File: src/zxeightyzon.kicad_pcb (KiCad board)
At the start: 2 copper layers, 77.6 x 75.9 mm, 0 parts

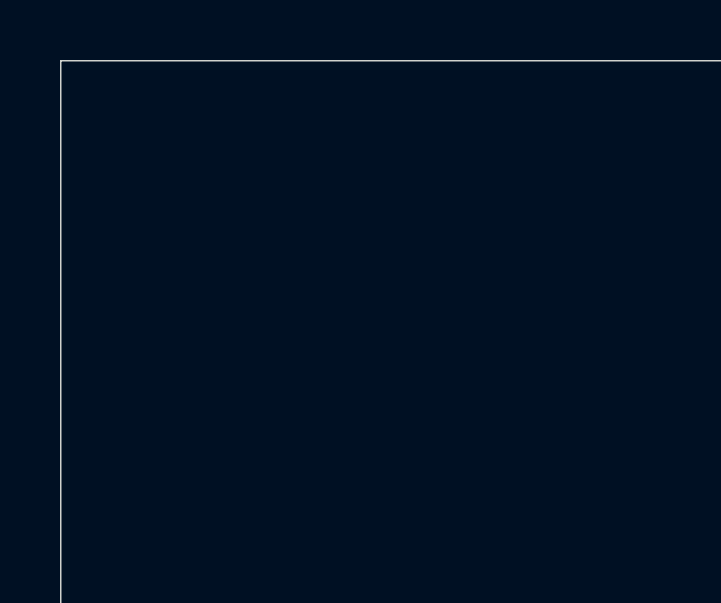
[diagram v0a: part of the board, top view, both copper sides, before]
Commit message: added logo footprint
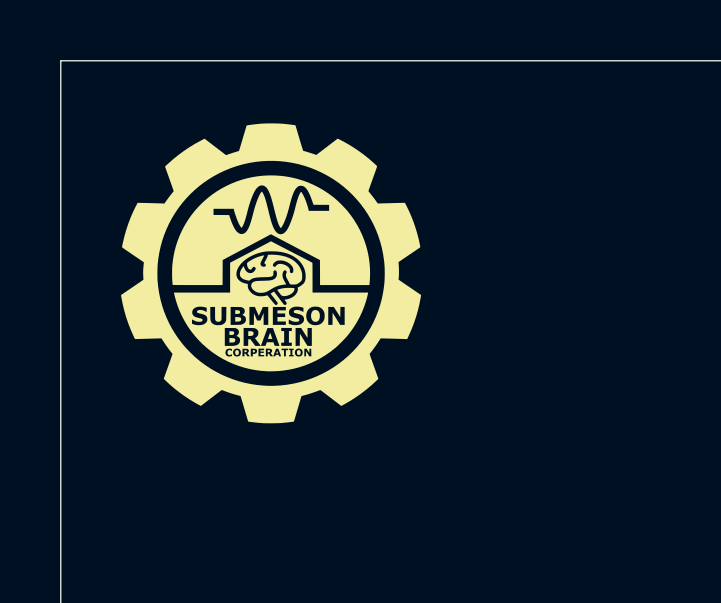
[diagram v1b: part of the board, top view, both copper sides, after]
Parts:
- added G***: LOGO, SBCLogo:SBCLogo, F.Cu at (57.7, 32.8)

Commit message: started PCB layout
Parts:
- added C1: 10uf, Capacitor_THT:CP_Radial_D5.0mm_P2.00mm, B.Cu at (218.8, 64.1)
- added C2: 10uf, Capacitor_THT:CP_Radial_D5.0mm_P2.00mm, B.Cu at (218.6, 54.0)
- added C3: 100nf, Capacitor_THT:C_Disc_D3.0mm_W1.6mm_P2.50mm, B.Cu at (238.3, 64.1)
- added C4: 100nf, Capacitor_THT:C_Disc_D3.0mm_W1.6mm_P2.50mm, B.Cu at (238.3, 54.0)
- added C5: 100nf, Capacitor_THT:C_Disc_D3.0mm_W1.6mm_P2.50mm, B.Cu at (199.9, 92.9)
- added C6: 100nf, Capacitor_THT:C_Disc_D3.0mm_W1.6mm_P2.50mm, B.Cu at (180.0, 108.3)
- added CO1: Connector ZX81, ZX81_Expansion_Connector:ZX81_EdgeConnector, F.Cu at (222.9, 104.3)
- added CO2: LINEOUT, audio_jack:CONN5_SPC21348_MTC, B.Cu at (244.3, 54.0)
- added FB1: FB, Resistor_THT:R_Axial_DIN0207_L6.3mm_D2.5mm_P7.62mm_Horizontal, B.Cu at (197.7, 77.7)
- added J1: 01x10, Connector_PinHeader_2.54mm:PinHeader_1x10_P2.54mm_Vertical, B.Cu at (250.8, 71.9)
- added J2: 01x10, Connector_PinHeader_2.54mm:PinHeader_1x10_P2.54mm_Vertical, B.Cu at (224.4, 71.9)
- added J3: 01x10, Connector_PinHeader_2.54mm:PinHeader_1x10_P2.54mm_Vertical, B.Cu at (198.0, 71.9)
- added J4: Conn_02x02_Top_Bottom, Connector_PinHeader_2.54mm:PinHeader_2x02_P2.54mm_Vertical, B.Cu at (197.1, 56.7)
- added JP1: YM 1/2 CLK, Connector_PinHeader_2.54mm:PinHeader_1x02_P2.54mm_Vertical, B.Cu at (194.2, 90.4)
- added JP2: CLK Select, Connector_PinHeader_2.54mm:PinHeader_1x03_P2.54mm_Vertical, B.Cu at (190.5, 90.4)
- added R2: 390R, Resistor_THT:R_Axial_DIN0207_L6.3mm_D2.5mm_P7.62mm_Horizontal, B.Cu at (205.3, 64.1)
- added R3: 390R, Resistor_THT:R_Axial_DIN0207_L6.3mm_D2.5mm_P7.62mm_Horizontal, B.Cu at (205.3, 54.0)
- added R4: 820R, Resistor_THT:R_Axial_DIN0207_L6.3mm_D2.5mm_P7.62mm_Horizontal, B.Cu at (212.9, 61.1)
- added R5: 820R, Resistor_THT:R_Axial_DIN0207_L6.3mm_D2.5mm_P7.62mm_Horizontal, B.Cu at (212.9, 57.0)
- added R6: 390R, Resistor_THT:R_Axial_DIN0207_L6.3mm_D2.5mm_P7.62mm_Horizontal, B.Cu at (226.7, 60.9)
- added R7: 390R, Resistor_THT:R_Axial_DIN0207_L6.3mm_D2.5mm_P7.62mm_Horizontal, B.Cu at (226.7, 57.0)
- added R8: 100R, Resistor_THT:R_Axial_DIN0207_L6.3mm_D2.5mm_P7.62mm_Horizontal, B.Cu at (226.7, 64.1)
- added R9: 100R, Resistor_THT:R_Axial_DIN0207_L6.3mm_D2.5mm_P7.62mm_Horizontal, B.Cu at (226.7, 54.0)
- added U1: YM2149, Package_DIP:DIP-40_W15.24mm_LongPads, B.Cu at (202.6, 77.7)
- added U2: GAL22V10, Package_DIP:DIP-24_W7.62mm_LongPads, B.Cu at (182.5, 77.7)
- G***: moved to B.Cu
- moved G*** 128.6 mm to (183.5, 59.4), turned to 180 degrees
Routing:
- net VCC: track 0.00 -> 181.2 mm
- net GND: track 0.00 -> 177.0 mm
- net /BDIR: track 0.00 -> 86.9 mm, vias 0 -> 1
- net /A7: track 0.00 -> 84.0 mm, vias 0 -> 2
- net GND_AUDIO: track 0.00 -> 83.6 mm, vias 0 -> 1
- net /A4: track 0.00 -> 82.5 mm, vias 0 -> 1
- net /A6: track 0.00 -> 79.9 mm, vias 0 -> 1
- net /A5: track 0.00 -> 76.6 mm, vias 0 -> 2
- net Net-(JP2-C): track 0.00 -> 62.4 mm
- net /~{RD}: track 0.00 -> 61.7 mm
- net /BC1: track 0.00 -> 59.7 mm
- net /A0: track 0.00 -> 57.0 mm, vias 0 -> 2
- net /CLK: track 0.00 -> 56.2 mm, vias 0 -> 1
- net /~{WR}: track 0.00 -> 54.8 mm
- net /A2: track 0.00 -> 54.6 mm, vias 0 -> 1
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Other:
- board size 77.6 x 75.9 mm -> 82.2 x 62 mm

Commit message: fab files
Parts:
- moved C2 134.5 mm to (84.9, 39.5)
- moved C6 134.5 mm to (46.2, 93.8)
- moved R6 134.5 mm to (93.0, 46.4)
- moved R7 134.5 mm to (93.0, 42.5)
- moved R8 134.5 mm to (93.0, 49.6)
- moved R9 134.5 mm to (93.0, 39.5)
- moved C3 134.5 mm to (104.5, 49.6)
- moved C4 134.5 mm to (104.5, 39.5)
- moved C5 134.5 mm to (66.2, 78.5)
- moved CO1 134.5 mm to (89.1, 89.8)
- moved FB1 134.5 mm to (64.0, 63.2)
- moved J2 134.5 mm to (90.7, 57.4)
- moved J3 134.5 mm to (64.3, 57.4)
- moved J4 134.5 mm to (63.4, 42.3)
- moved JP1 134.5 mm to (60.4, 75.9)
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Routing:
- net /A7: track 84.0 -> 63.9 mm, vias 2 -> 0
- net /BDIR: track 86.9 -> 68.2 mm
- net VCC: track 181.2 -> 194.2 mm
- net /D5: track 26.1 -> 17.8 mm
- net /A5: track 76.6 -> 69.9 mm, vias 2 -> 0
- net /D3: track 9.82 -> 16.3 mm
- net /IOA0: track 23.1 -> 29.0 mm
- net /A6: track 79.9 -> 85.7 mm
- net Net-(J4-Pin_2): track 6.75 -> 11.6 mm
- net /A0: track 57.0 -> 52.2 mm, vias 2 -> 1
- net /IOA4: track 12.7 -> 7.95 mm
- net /IOA2: track 12.7 -> 7.95 mm
- net /IOA7: track 8.38 -> 12.7 mm
- net /A2: track 54.6 -> 50.6 mm
- net /IOA5: track 11.4 -> 7.95 mm
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
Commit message: Added silkscreen overlays
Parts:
- J1 I/O-A: renamed from J1
- J2 I/O-B: renamed from J2
- J3 GAL: renamed from J3
- moved G*** 5.03 mm to (45.2, 42.8)
- renumbered J4 to ABC↓, JP2 to CLK, JP1 to SEL
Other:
- board text added: "ACB→"
- board text added: "CLK/2"
- board text added: "ZXEightyZON rev 1.0 Designed by Bambleweeny57 for Submeson Brain Corporation"
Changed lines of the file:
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@@
 		(descr "Through hole straight pin header, 2x02, 2.54mm pitch, double rows")
 		(tags "Through hole pin header THT 2x02 2.54mm double row")
-		(property "Reference" "J4"
-			(at 1.397 2.413 0)
+		(property "Reference" "ABC↓"
+			(at 1.1094 2.4914 0)
 			(layer "B.SilkS")
 			(effects
@@
 		(descr "Through hole straight pin header, 1x02, 2.54mm pitch, single row")
 		(tags "Through hole pin header THT 1x02 2.54mm single row")
-		(property "Reference" "JP1"
+		(property "Reference" "SEL"
 			(at 0 2.54 0)
 			(layer "B.SilkS")
@@
 		(descr "Through hole straight pin header, 1x10, 2.54mm pitch, single row")
 		(tags "Through hole pin header THT 1x10 2.54mm single row")
-		(property "Reference" "J2"
-			(at 2.413 0 0)
+		(property "Reference" "J2 I/O-B"
+			(at 2.3932 -2.4202 0)
 			(layer "B.SilkS")
 			(effects
@@
 		(descr "Through hole straight pin header, 1x10, 2.54mm pitch, single row")
 		(tags "Through hole pin header THT 1x10 2.54mm single row")
-		(property "Reference" "J1"
-			(at 2.413 0 0)
+		(property "Reference" "J1 I/O-A"
+			(at 2.3932 -2.3362 0)
 			(layer "B.SilkS")
 			(effects
@@
 		(descr "Through hole straight pin header, 1x10, 2.54mm pitch, single row")
 		(tags "Through hole pin header THT 1x10 2.54mm single row")
-		(property "Reference" "J3"
-			(at 2.413 0 0)
+		(property "Reference" "J3 GAL"
+			(at 2.3932 -1.2542 0)
 			(layer "B.SilkS")
 			(effects
@@
 	(footprint "SBCLogo:SBCLogo"
 		(layer "B.Cu")
-		(at 49.7762 44.9472 180)
+		(at 45.25 42.75 180)
 		(property "Reference" "G***"
 			(at 0 0 0)
@@
 		(descr "Through hole straight pin header, 1x03, 2.54mm pitch, single row")
 		(tags "Through hole pin header THT 1x03 2.54mm single row")
-		(property "Reference" "JP2"
+		(property "Reference" "CLK"
 			(at 0 2.54 0)
 			(layer "B.SilkS")
@@
 		(layer "Edge.Cuts")
 	)
+	(gr_text "ACB→"
+		(at 66.25 37.75 0)
+		(layer "B.SilkS")
+		(effects
+			(font
+				(size 1 1)
+				(thickness 0.15)
+			)
+			(justify left bottom mirror)
+		)
+	)
+	(gr_text "CLK/2"
+		(at 58.25 84 0)
+		(layer "B.SilkS")
+		(effects
+			(font
+				(size 1 1)
+				(thickness 0.15)
+			)
+			(justify left bottom mirror)
+		)
+	)
+	(gr_text "ZXEightyZON rev 1.0\nDesigned by Bambleweeny57\nfor Submeson Brain Corporation"
+		(at 67 52 0)
+		(layer "B.SilkS")
+		(effects
+			(font
+				(size 1 1)
+				(thickness 0.1)
+			)
+			(justify left bottom mirror)
+		)
+	)
 	(segment

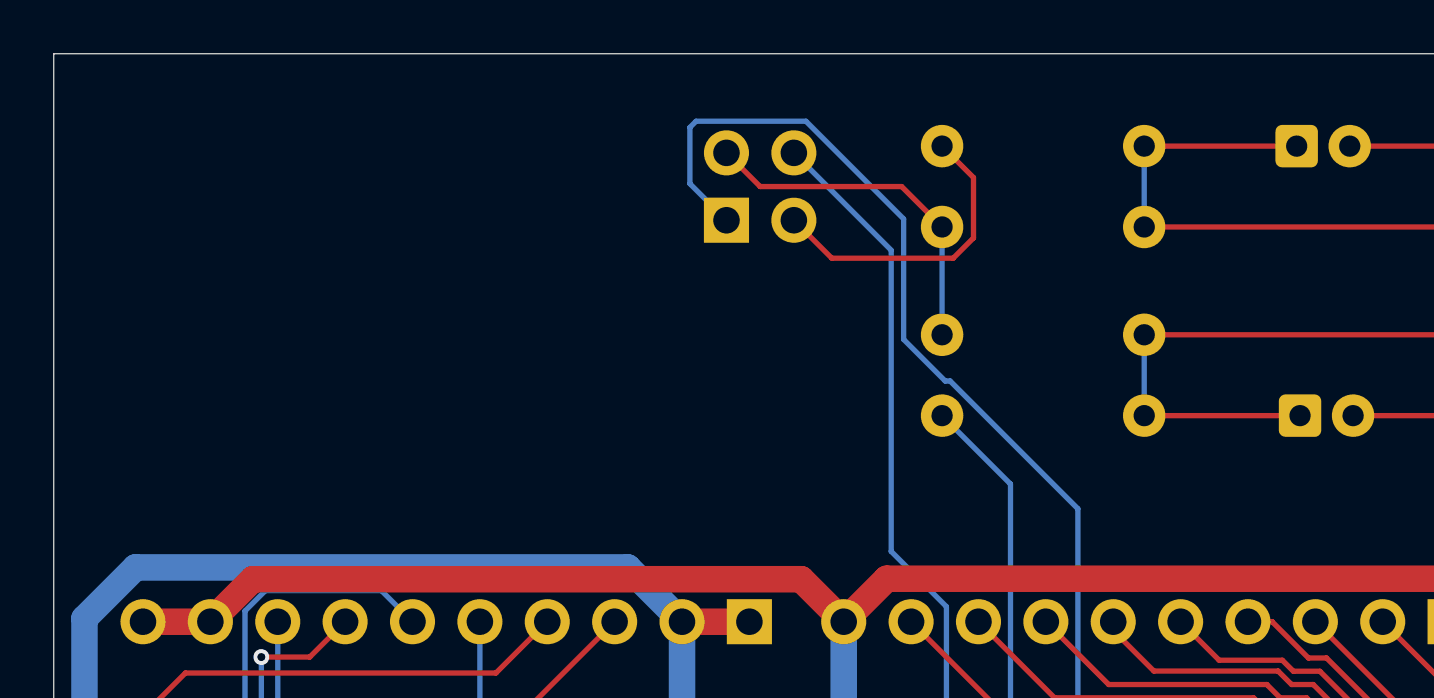
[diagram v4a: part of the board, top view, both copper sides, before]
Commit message: Added Open Hardware Silk Screen
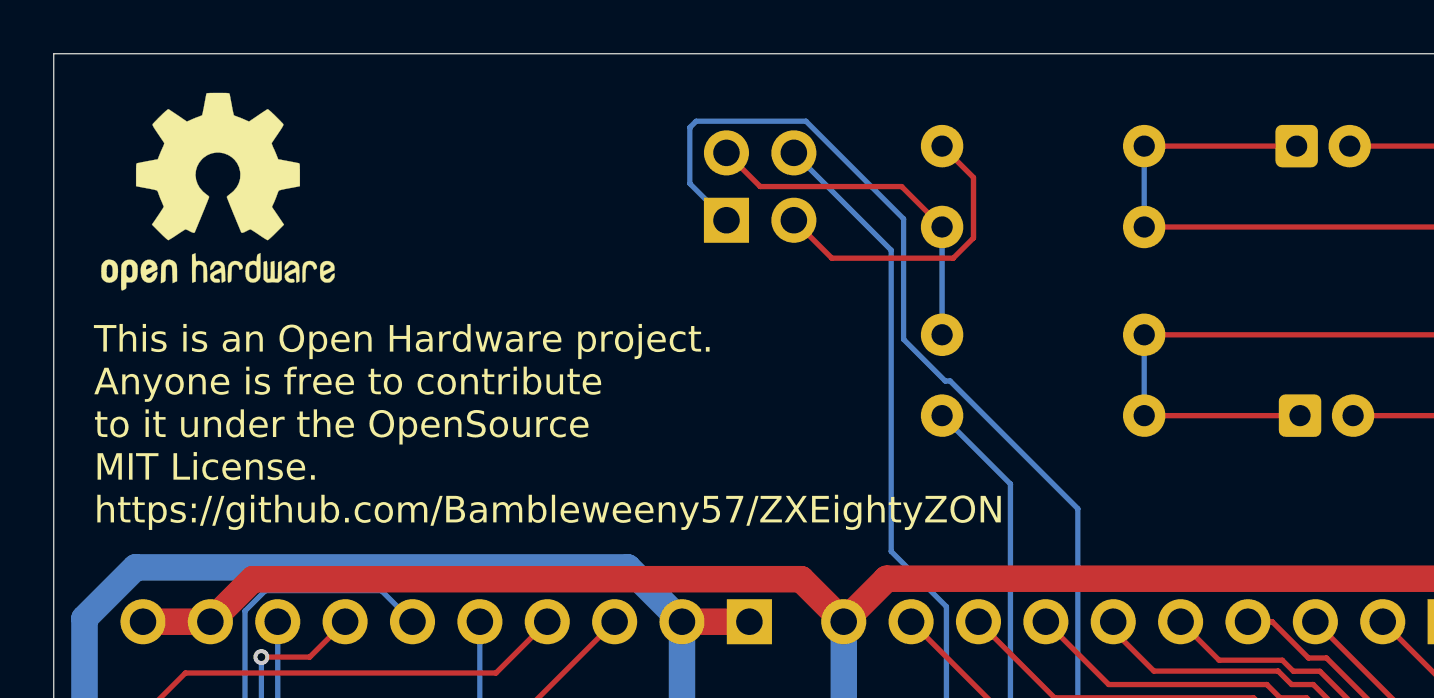
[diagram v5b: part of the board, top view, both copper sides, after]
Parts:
- added REF**: OSHW-Logo2_9.8x8mm_SilkScreen, Symbol:OSHW-Logo2_9.8x8mm_SilkScreen, F.Cu at (44.2, 41.2)
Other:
- board text added: "This is an Open Hardware project. Anyone is free to contribute to it under the OpenSource MIT License. https://github.com/Bambleweeny57/ZXEightyZON"

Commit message: Added IO Silk Screen Overlay
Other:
- board text added: "A0"
- board text added: "A1"
- board text added: "A2"
- board text added: "A3"
- board text added: "A4"
- board text added: "A5"
- board text added: "A6"
- board text added: "A7"
- board text added: "B0"
- board text added: "B1"
- board text added: "B2"
- board text added: "B3"
- board text added: "B4"
- board text added: "B5"
- board text added: "B6"
- board text added: "B7"
- board text added: "GND"
- board text added: "O0"
- board text added: "O1"
- board text added: "O2"
- board text added: "O3"
- board text added: "O4"
- board text added: "O5"
- board text added: "VCC"

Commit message: Re rooted IO A
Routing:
- net /IOA7: track 12.7 -> 7.95 mm
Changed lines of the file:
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@@
 	)
 	(segment
-		(start 98.0975 58.7245)
-		(end 96.7662 57.3932)
+		(start 101.8462 62.4732)
+		(end 101.8462 63.2352)
 		(width 0.2)
 		(layer "B.Cu")
@@
 	)
 	(segment
-		(start 101.8462 64.7369)
-		(end 98.8339 64.7369)
+		(start 96.7662 57.3932)
+		(end 101.8462 62.4732)
 		(width 0.2)
 		(layer "B.Cu")
-		(net 56)
-	)
-	(segment
-		(start 101.8462 63.2352)
-		(end 101.8462 64.7369)
-		(width 0.2)
-		(layer "B.Cu")
-		(net 56)
-	)
-	(segment
-		(start 98.8339 64.7369)
-		(end 98.0975 64.0005)
-		(width 0.2)
-		(layer "B.Cu")
-		(net 56)
-	)
-	(segment
-		(start 98.0975 64.0005)
-		(end 98.0975 58.7245)
-		(width 0.2)
-		(layer "B.Cu")
